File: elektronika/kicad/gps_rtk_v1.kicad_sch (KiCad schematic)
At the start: 0 parts

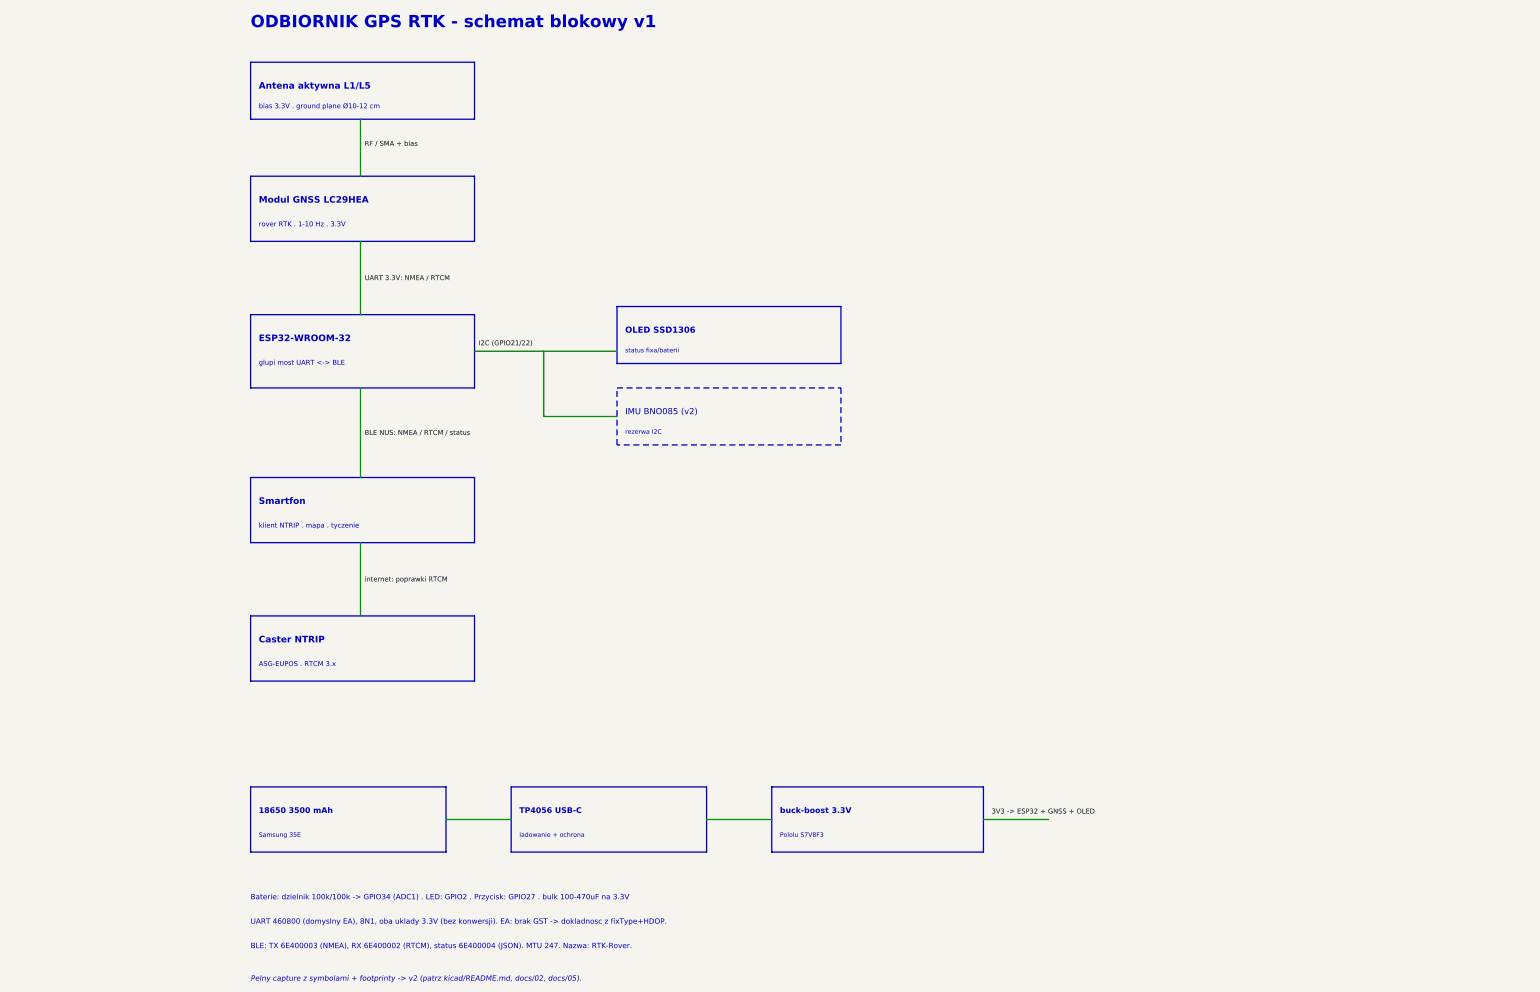
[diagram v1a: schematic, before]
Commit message: elektronika/kicad: pelny schemat z symbolami (netlista zweryfikowana)
- gps_rtk_v1.kicad_sch: schemat blokowy -> pelny schemat z prawdziwymi symbolami KiCad
  (ESP32-WROOM-32, zlacza GNSS/OLED/IMU/TP4056/buck, dzielnik, pull-upy I2C, LED, przycisk, C)
- polaczenia po nazwach netow; zweryfikowane przez kicad-cli sch export netlist (15 netow OK)
- generator gen/gen_schematic.py (kiutils + biblioteki symboli KiCad 9)
- re-eksport gps_rtk_v1.pdf + gps_rtk_v1.svg
- ERC w kicad-cli crashuje (quirk kiutils); weryfikacja netlista, ERC w GUI po zapisie

Co-Authored-By: Claude Opus 4.8 (1M context) <noreply@anthropic.com>
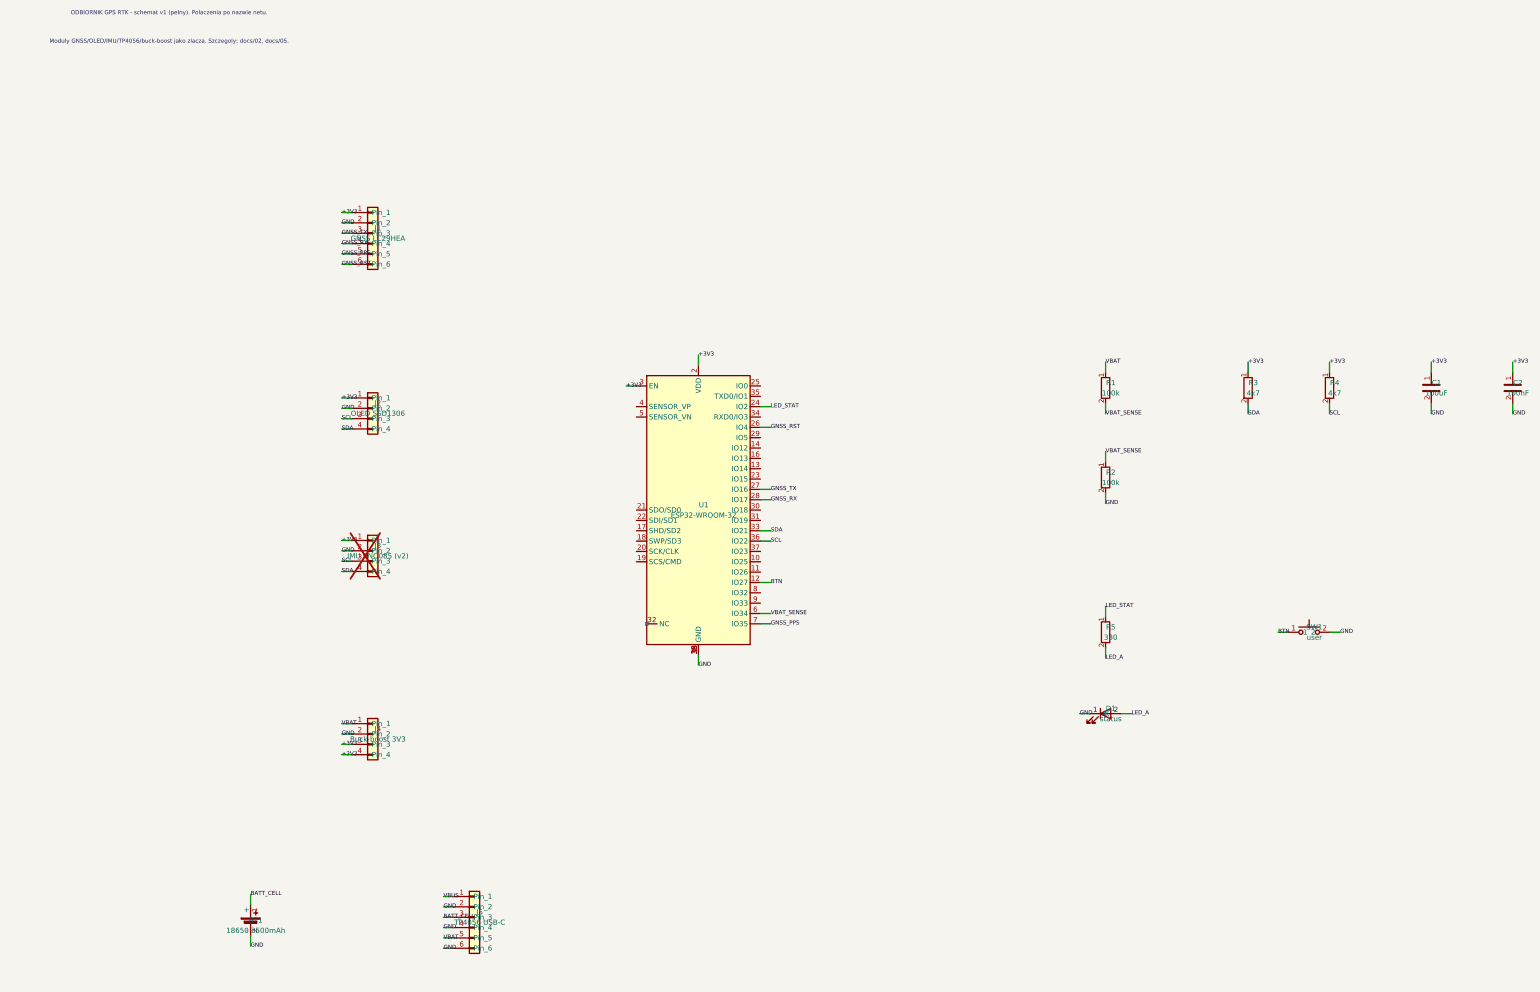
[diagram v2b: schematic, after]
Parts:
- added BT1: 18650 3500mAh, symbol Device:Battery_Cell
- added C1: 100uF, symbol Device:C
- added C2: 100nF, symbol Device:C
- added D1: status, symbol Device:LED
- added J1: GNSS LC29HEA, symbol Connector_Generic:Conn_01x06
- added J2: OLED SSD1306, symbol Connector_Generic:Conn_01x04
- added J3: IMU BNO085 (v2), symbol Connector_Generic:Conn_01x04
- added J4: Buck-boost 3V3, symbol Connector_Generic:Conn_01x04
- added J5: TP4056 USB-C, symbol Connector_Generic:Conn_01x06
- added R1, R2: 100k, symbol Device:R
- added R3, R4: 4k7, symbol Device:R
- added R5: 330, symbol Device:R
- added SW1: user, symbol Switch:SW_Push
- added U1: ESP32-WROOM-32, symbol RF_Module:ESP32-WROOM-32
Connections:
- new net +3V3: C1.1, C2.1, J1.1 (Pin_1), J2.1 (Pin_1), J3.1 (Pin_1), J4.3 (Pin_3), J4.4 (Pin_4), R3.1, R4.1, U1.2 (VDD), U1.3 (EN)
- new net BATT_CELL: BT1.1 (+), J5.3 (Pin_3)
- new net BTN: SW1.1, U1.12 (IO27)
- new net GND: BT1.2 (-), C1.2, C2.2, D1.1 (K), J1.2 (Pin_2), J2.2 (Pin_2), J3.2 (Pin_2), J4.2 (Pin_2), J5.2 (Pin_2), J5.4 (Pin_4), J5.6 (Pin_6), R2.2, SW1.2, U1.1 (GND), U1.15 (GND), U1.38 (GND), U1.39 (GND)
- new net GNSS_PPS: J1.5 (Pin_5), U1.7 (IO35)
- new net GNSS_RST: J1.6 (Pin_6), U1.26 (IO4)
- new net GNSS_RX: J1.4 (Pin_4), U1.28 (IO17)
- new net GNSS_TX: J1.3 (Pin_3), U1.27 (IO16)
- new net LED_A: D1.2 (A), R5.2
- new net LED_STAT: R5.1, U1.24 (IO2)
- new net SCL: J2.3 (Pin_3), J3.3 (Pin_3), R4.2, U1.36 (IO22)
- new net SDA: J2.4 (Pin_4), J3.4 (Pin_4), R3.2, U1.33 (IO21)
- new net VBAT: J4.1 (Pin_1), J5.5 (Pin_5), R1.1
- new net VBAT_SENSE: R1.2, R2.1, U1.6 (IO34)
- new net VBUS: J5.1 (Pin_1)
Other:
- note added: "Moduly GNSS/OLED/IMU/TP4056/buck-boost jako zlacza. Szczegoly: docs/02, docs/05."
- note added: "ODBIORNIK GPS RTK - schemat v1 (pelny). Polaczenia po nazwie netu."
- note removed: "18650 3500 mAh"
- note removed: "ASG-EUPOS . RTCM 3.x"
- note removed: "Antena aktywna L1/L5"
- note removed: "BLE: TX 6E400003 (NMEA), RX 6E400002 (RTCM), status 6E400004 (JSON). MTU 247. Nazwa: RTK-Rover."
- note removed: "Baterie: dzielnik 100k/100k -> GPIO34 (ADC1) . LED: GPIO2 . Przycisk: GPIO27 . bulk 100-470uF na 3.3V"
- note removed: "Caster NTRIP"
- note removed: "ESP32-WROOM-32"
- note removed: "IMU BNO085 (v2)"
- note removed: "Modul GNSS LC29HEA"
- note removed: "ODBIORNIK GPS RTK - schemat blokowy v1"
- note removed: "OLED SSD1306"
- note removed: "Pelny capture z symbolami + footprinty -> v2 (patrz kicad/README.md, docs/02, docs/05)."
- note removed: "Pololu S7V8F3"
- note removed: "Samsung 35E"
- note removed: "Smartfon"
- note removed: "TP4056 USB-C"
- note removed: "UART 460800 (domyslny EA), 8N1, oba uklady 3.3V (bez konwersji). EA: brak GST -> dokladnosc z fixType+HDOP."
- note removed: "bias 3.3V . ground plane Ø10-12 cm"
- note removed: "buck-boost 3.3V"
- note removed: "glupi most UART <-> BLE"
- note removed: "klient NTRIP . mapa . tyczenie"
- note removed: "ladowanie + ochrona"
- note removed: "rezerwa I2C"
- note removed: "rover RTK . 1-10 Hz . 3.3V"
- note removed: "status fixa/baterii"
